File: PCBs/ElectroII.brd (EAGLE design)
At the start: 114.3 x 76.2 mm, 30 parts, among them J1 U.FL-R-SMT(01), U1 RFM95W-868S2, U2 TPS61090RSAR

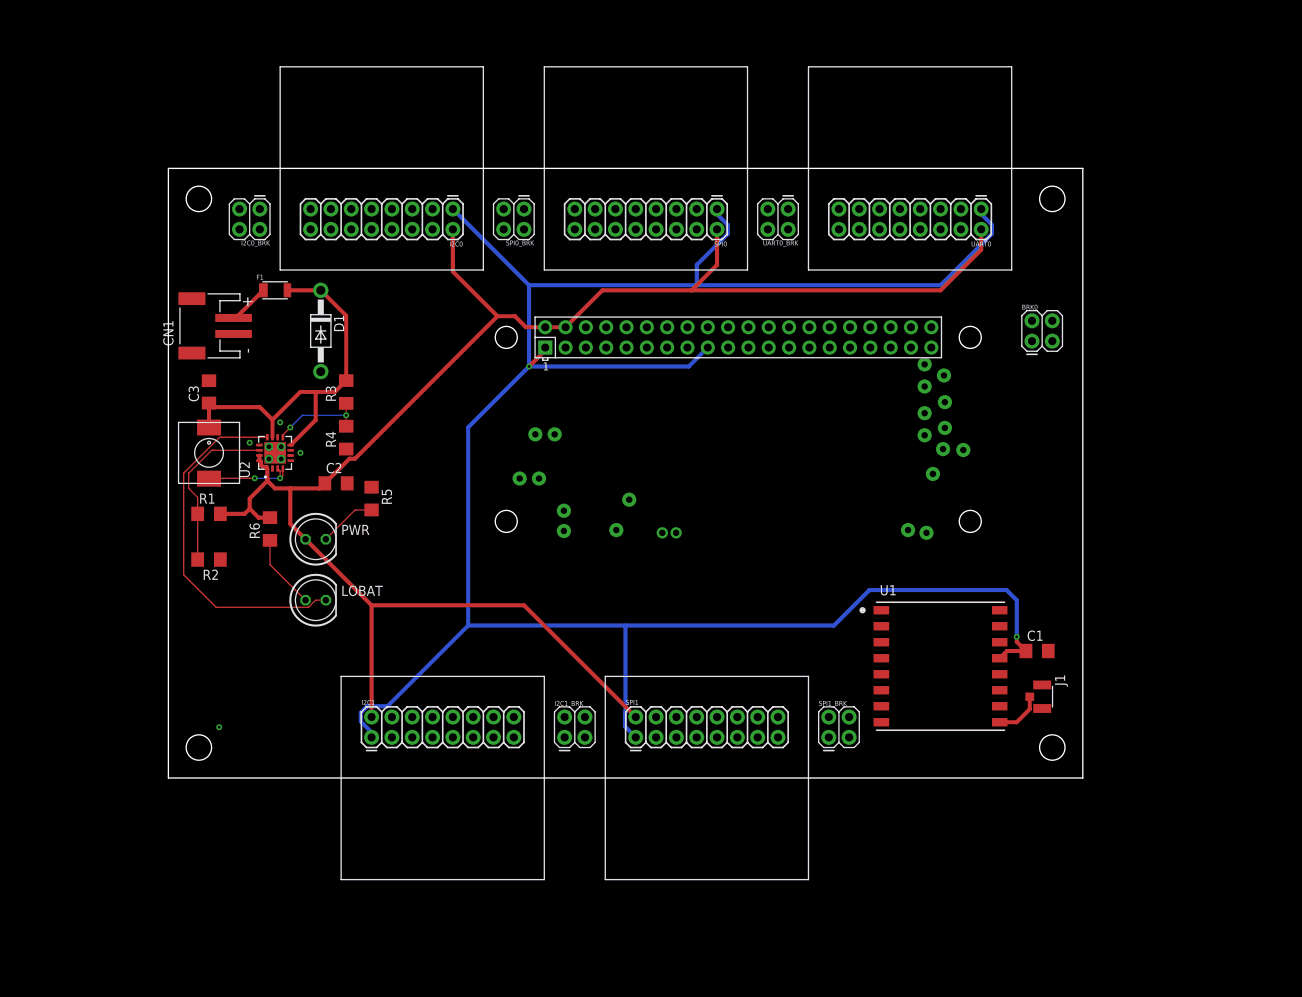
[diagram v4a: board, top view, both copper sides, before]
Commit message: Added sample pins and new trace ideas
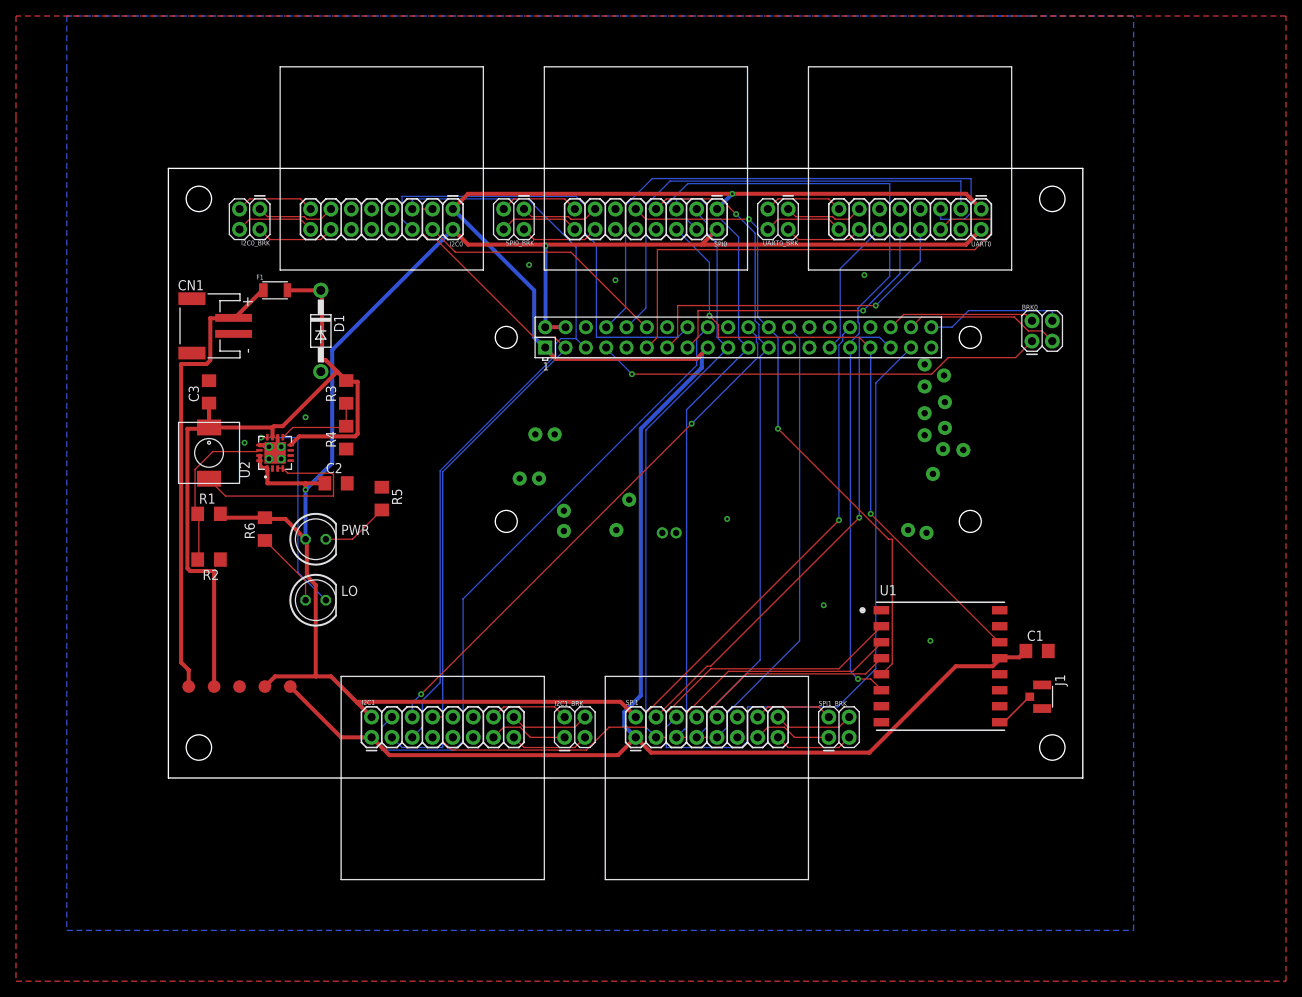
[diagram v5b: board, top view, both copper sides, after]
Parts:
- added T1: VIN, RTR Main Library:TEST_PAD
- added T2: VBAT, RTR Main Library:TEST_PAD
- added T3: GND, RTR Main Library:TEST_PAD
- added T4: 5V, RTR Main Library:TEST_PAD
- added T5: VCC, RTR Main Library:TEST_PAD
- R5, R6: value (none) -> 220
- moved R5 1.27 mm to (26.7, 34.9)
- moved R6 0.63 mm to (12.1, 31.1)
- renumbered LOBAT to LO
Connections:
- net 5V: now also T4.P$1
- net GND: now also T3.P$1
- net VBAT: now also T2.P$1
- net VCC: now also T5.P$1
- net VIN: now also T1.P$1
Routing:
- net MISO: track 0.00 -> 111.2 mm
- net SCLK: track 0.00 -> 111.1 mm, vias 0 -> 1
- net MOSI: track 0.00 -> 108.2 mm
- net SPI0_GPIO0: track 0.00 -> 103.2 mm, vias 0 -> 1
- net SCL: track 0.00 -> 96.8 mm
- net I2C1_GPIO2: track 0.00 -> 91.9 mm, vias 0 -> 1
- net SDA: track 0.00 -> 91.3 mm
- net CE0: track 0.00 -> 79.9 mm, vias 0 -> 2
- net I2C1_GPIO0: track 0.00 -> 79.7 mm
- net SPI1_GPIO1: track 0.00 -> 79.1 mm
- net SPI0_GPIO1: track 0.00 -> 78.8 mm, vias 0 -> 2
- net TX: track 0.00 -> 70.5 mm
- net I2C1_GPIO1: track 0.00 -> 67.1 mm, vias 0 -> 2
- net UART0_GPIO0: track 0.00 -> 64.0 mm
- net SPI1_GPIO0: track 0.00 -> 62.7 mm, vias 0 -> 1
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- added copper zone on layer 1, net GND
- added copper zone on layer 16, net GND
